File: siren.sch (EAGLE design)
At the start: 10 parts, among them IC1 UM3561, T1 BC547

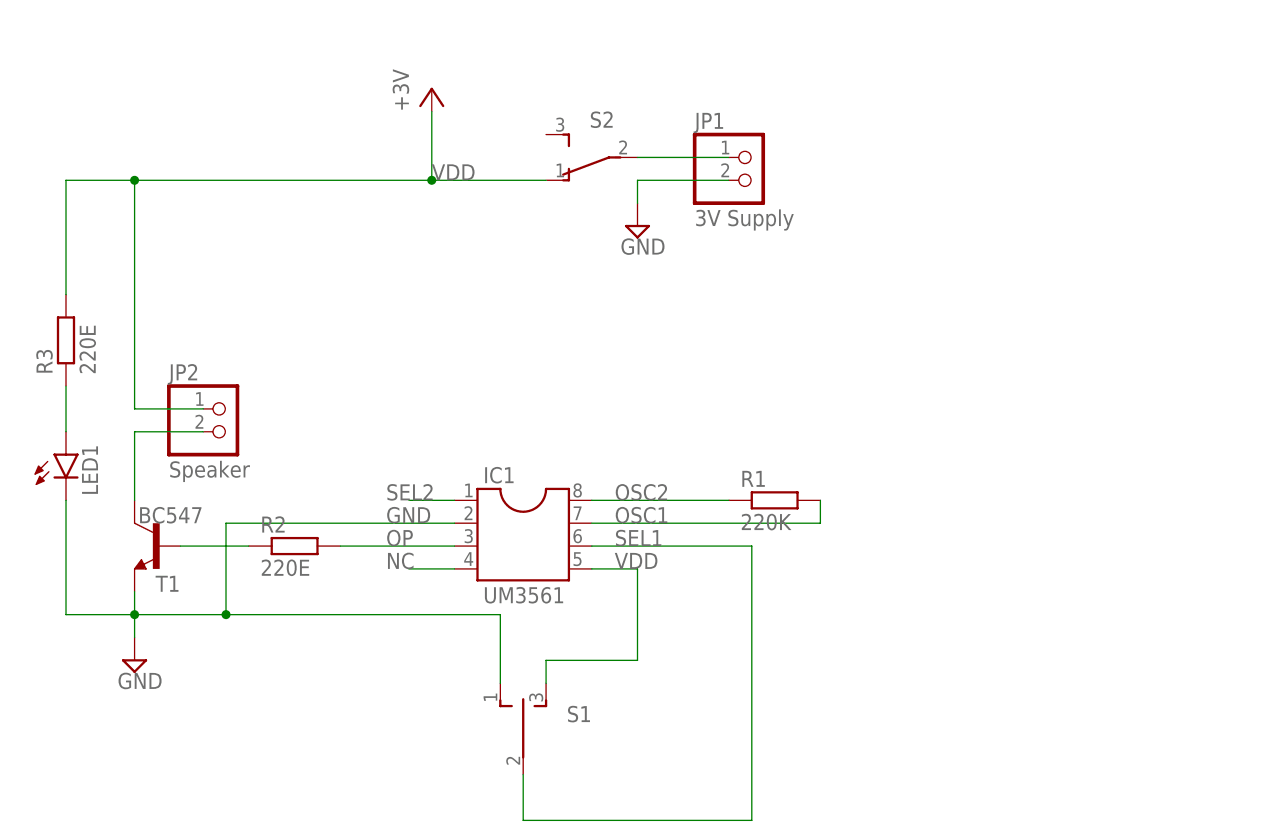
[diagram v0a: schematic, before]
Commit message: SP3T replaced with 5 header pins
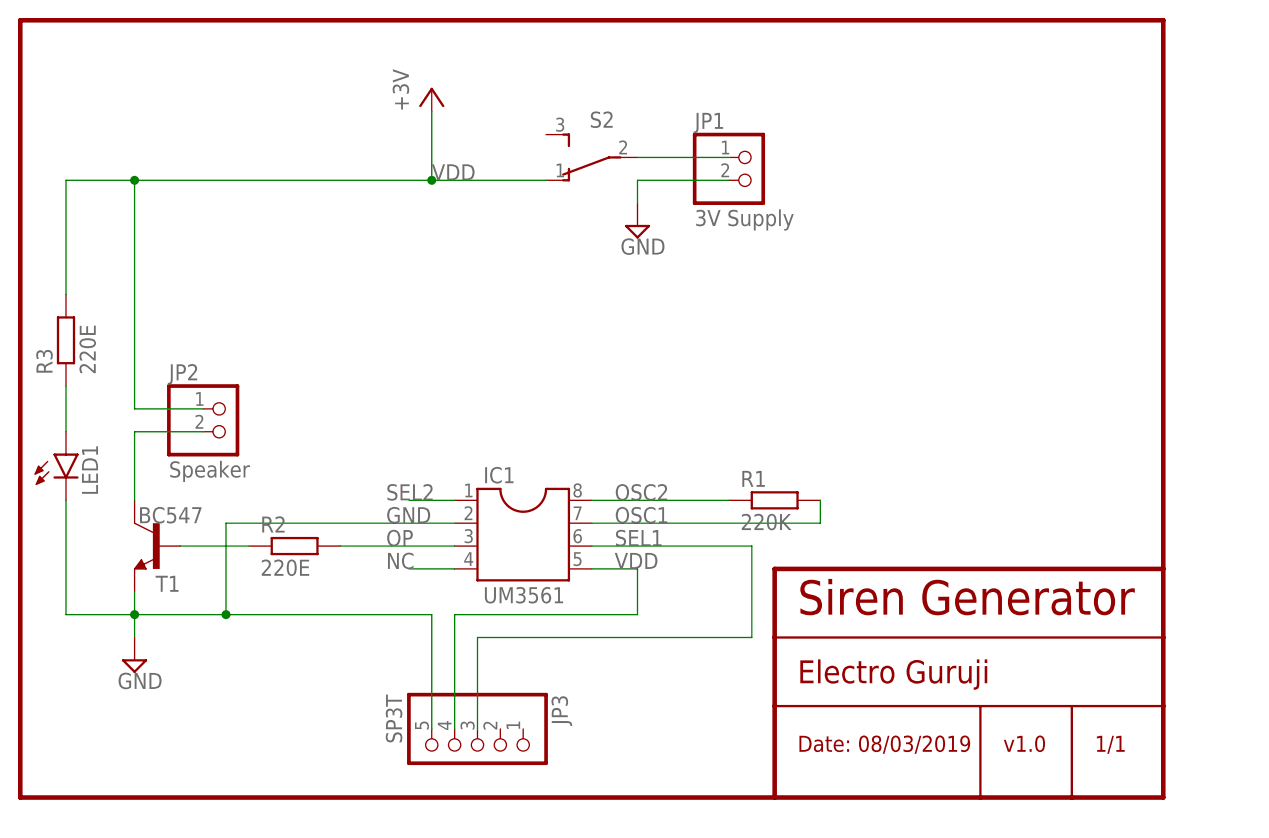
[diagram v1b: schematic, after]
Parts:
- removed S1: TL39YO, switch:TL39YO
- added JP3: SP3T, pinhead:PINHD-1X5
- JP1: SPICEPREFIX (none) -> B
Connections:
- net GND: now also JP3.5; no longer S1.O
- net SEL1: now also JP3.3; no longer S1.P
- net VDD: now also JP3.4; no longer S1.S
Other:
- note added: "1/1"
- note added: "Date: 08/03/2019"
- note added: "Electro Guruji"
- note added: "Siren Generator"
- note added: "v1.0"
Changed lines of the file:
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@@
 <part name="R2" library="resistor" library_urn="urn:adsk.eagle:library:348" deviceset="R-EU_" device="0204/5" package3d_urn="urn:adsk.eagle:package:23488/1" value="220E"/>
 <part name="T1" library="transistor" library_urn="urn:adsk.eagle:library:402" deviceset="*-NPN-" device="TO92-EBC" package3d_urn="urn:adsk.eagle:package:29915/2" value="BC547"/>
-<part name="JP1" library="pinhead" library_urn="urn:adsk.eagle:library:325" deviceset="PINHD-1X2" device="" package3d_urn="urn:adsk.eagle:package:22435/2" value="3V Supply"/>
+<part name="JP1" library="pinhead" library_urn="urn:adsk.eagle:library:325" deviceset="PINHD-1X2" device="" package3d_urn="urn:adsk.eagle:package:22435/2" value="3V Supply">
+<attribute name="SPICEPREFIX" value="B"/>
+</part>
 <part name="JP2" library="pinhead" library_urn="urn:adsk.eagle:library:325" deviceset="PINHD-1X2" device="" package3d_urn="urn:adsk.eagle:package:22435/2" value="Speaker"/>
 <part name="R3" library="resistor" library_urn="urn:adsk.eagle:library:348" deviceset="R-EU_" device="0204/5" package3d_urn="urn:adsk.eagle:package:23488/1" value="220E"/>
 <part name="LED1" library="led" library_urn="urn:adsk.eagle:library:259" deviceset="LED" device="5MM" package3d_urn="urn:adsk.eagle:package:15799/2"/>
-<part name="S1" library="switch" library_urn="urn:adsk.eagle:library:380" deviceset="TL39YO" device="" package3d_urn="urn:adsk.eagle:package:27747/1"/>
 <part name="S2" library="switch" library_urn="urn:adsk.eagle:library:380" deviceset="TL36YO" device="" package3d_urn="urn:adsk.eagle:package:27747/1"/>
 <part name="SUPPLY1" library="supply2" library_urn="urn:adsk.eagle:library:372" deviceset="GND" device=""/>
 <part name="+3V" library="supply1" library_urn="urn:adsk.eagle:library:371" deviceset="VCC" device="" value="+3V"/>
 <part name="SUPPLY2" library="supply2" library_urn="urn:adsk.eagle:library:372" deviceset="GND" device=""/>
+<part name="JP3" library="pinhead" library_urn="urn:adsk.eagle:library:325" deviceset="PINHD-1X5" device="" package3d_urn="urn:adsk.eagle:package:22469/2" value="SP3T"/>
 </parts>
 <sheets>
 <sheet>
 <plain>
+<wire x1="132.08" y1="152.4" x2="132.08" y2="66.04" width="0.508" layer="94"/>
+<wire x1="132.08" y1="66.04" x2="215.9" y2="66.04" width="0.508" layer="94"/>
+<wire x1="215.9" y1="66.04" x2="238.76" y2="66.04" width="0.508" layer="94"/>
+<wire x1="238.76" y1="66.04" x2="248.92" y2="66.04" width="0.508" layer="94"/>
+<wire x1="248.92" y1="66.04" x2="259.08" y2="66.04" width="0.508" layer="94"/>
+<wire x1="259.08" y1="66.04" x2="259.08" y2="76.2" width="0.508" layer="94"/>
+<wire x1="259.08" y1="76.2" x2="259.08" y2="83.82" width="0.508" layer="94"/>
+<wire x1="259.08" y1="83.82" x2="259.08" y2="91.44" width="0.508" layer="94"/>
+<wire x1="259.08" y1="91.44" x2="259.08" y2="152.4" width="0.508" layer="94"/>
+<wire x1="259.08" y1="152.4" x2="132.08" y2="152.4" width="0.508" layer="94"/>
+<wire x1="215.9" y1="66.04" x2="215.9" y2="76.2" width="0.508" layer="94"/>
+<wire x1="215.9" y1="76.2" x2="215.9" y2="83.82" width="0.508" layer="94"/>
+<wire x1="215.9" y1="83.82" x2="215.9" y2="91.44" width="0.508" layer="94"/>
+<wire x1="215.9" y1="91.44" x2="259.08" y2="91.44" width="0.508" layer="94"/>
+<text x="218.44" y="86.36" size="3.81" layer="94">Siren Generator</text>
+<text x="218.44" y="78.74" size="2.54" layer="94">Electro Guruji</text>
+<wire x1="215.9" y1="83.82" x2="259.08" y2="83.82" width="0.254" layer="94"/>
+<wire x1="215.9" y1="76.2" x2="238.76" y2="76.2" width="0.254" layer="94"/>
+<text x="218.44" y="71.12" size="1.778" layer="94">Date: 08/03/2019</text>
+<wire x1="238.76" y1="76.2" x2="248.92" y2="76.2" width="0.254" layer="94"/>
+<wire x1="248.92" y1="76.2" x2="259.08" y2="76.2" width="0.254" layer="94"/>
+<wire x1="238.76" y1="76.2" x2="238.76" y2="66.04" width="0.254" layer="94"/>
+<text x="241.3" y="71.12" size="1.778" layer="94">v1.0</text>
+<wire x1="248.92" y1="76.2" x2="248.92" y2="66.04" width="0.254" layer="94"/>
+<text x="251.46" y="71.12" size="1.778" layer="94">1/1</text>
 </plain>
 <instances>
@@
 <attribute name="VALUE" x="142.875" y="99.568" size="1.778" layer="96" rot="R90"/>
 </instance>
-<instance part="S1" gate="BEF1" x="187.96" y="73.66" smashed="yes">
-<attribute name="NAME" x="195.58" y="76.2" size="1.778" layer="95" rot="R180"/>
-</instance>
 <instance part="S2" gate="BEF1" x="195.58" y="137.16" smashed="yes" rot="R90">
 <attribute name="NAME" x="198.12" y="142.24" size="1.778" layer="95" rot="R180"/>
@@
 <instance part="SUPPLY2" gate="GND" x="200.66" y="129.54" smashed="yes">
 <attribute name="VALUE" x="198.755" y="126.365" size="1.778" layer="96"/>
+</instance>
+<instance part="JP3" gate="A" x="182.88" y="71.12" smashed="yes" rot="R270">
+<attribute name="NAME" x="191.135" y="77.47" size="1.778" layer="95" rot="R270"/>
+<attribute name="VALUE" x="172.72" y="77.47" size="1.778" layer="96" rot="R270"/>
 </instance>
 </instances>
@@
 <label x="198.12" y="93.98" size="1.778" layer="95"/>
 <wire x1="195.58" y1="93.98" x2="213.36" y2="93.98" width="0.1524" layer="91"/>
-<wire x1="213.36" y1="93.98" x2="213.36" y2="63.5" width="0.1524" layer="91"/>
-<wire x1="213.36" y1="63.5" x2="187.96" y2="63.5" width="0.1524" layer="91"/>
-<pinref part="S1" gate="BEF1" pin="P"/>
-<wire x1="187.96" y1="63.5" x2="187.96" y2="68.58" width="0.1524" layer="91"/>
+<pinref part="JP3" gate="A" pin="3"/>
+<wire x1="182.88" y1="73.66" x2="182.88" y2="83.82" width="0.1524" layer="91"/>
+<wire x1="182.88" y1="83.82" x2="213.36" y2="83.82" width="0.1524" layer="91"/>
+<wire x1="213.36" y1="83.82" x2="213.36" y2="93.98" width="0.1524" layer="91"/>
 </segment>
 </net>
@@
 <pinref part="LED1" gate="G$1" pin="C"/>
 <wire x1="137.16" y1="86.36" x2="137.16" y2="99.06" width="0.1524" layer="91"/>
-<pinref part="S1" gate="BEF1" pin="O"/>
-<wire x1="154.94" y1="86.36" x2="185.42" y2="86.36" width="0.1524" layer="91"/>
-<wire x1="185.42" y1="86.36" x2="185.42" y2="78.74" width="0.1524" layer="91"/>
+<pinref part="JP3" gate="A" pin="5"/>
+<wire x1="154.94" y1="86.36" x2="177.8" y2="86.36" width="0.1524" layer="91"/>
+<wire x1="177.8" y1="86.36" x2="177.8" y2="73.66" width="0.1524" layer="91"/>
 <junction x="154.94" y="86.36"/>
 </segment>
@@
 <wire x1="195.58" y1="91.44" x2="200.66" y2="91.44" width="0.1524" layer="91"/>
 <label x="198.12" y="91.44" size="1.778" layer="95"/>
-<wire x1="200.66" y1="91.44" x2="200.66" y2="81.28" width="0.1524" layer="91"/>
-<wire x1="200.66" y1="81.28" x2="190.5" y2="81.28" width="0.1524" layer="91"/>
-<pinref part="S1" gate="BEF1" pin="S"/>
-<wire x1="190.5" y1="81.28" x2="190.5" y2="78.74" width="0.1524" layer="91"/>
-</segment>
-<segment>
+<wire x1="200.66" y1="91.44" x2="200.66" y2="86.36" width="0.1524" layer="91"/>
+<wire x1="200.66" y1="86.36" x2="180.34" y2="86.36" width="0.1524" layer="91"/>
+<pinref part="JP3" gate="A" pin="4"/>
+<wire x1="180.34" y1="86.36" x2="180.34" y2="73.66" width="0.1524" layer="91"/>
+</segment>
+<segment>
